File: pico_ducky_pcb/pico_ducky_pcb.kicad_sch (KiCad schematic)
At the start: 32 parts, among them J1 USB_A, J2 Conn_01x03_Female, SW1 R-667799, SW2 R-667799, U1 AP2127K-3.3, U2 W25Q32JVZP, U3 RP2040, Y1 Crystal_GND24

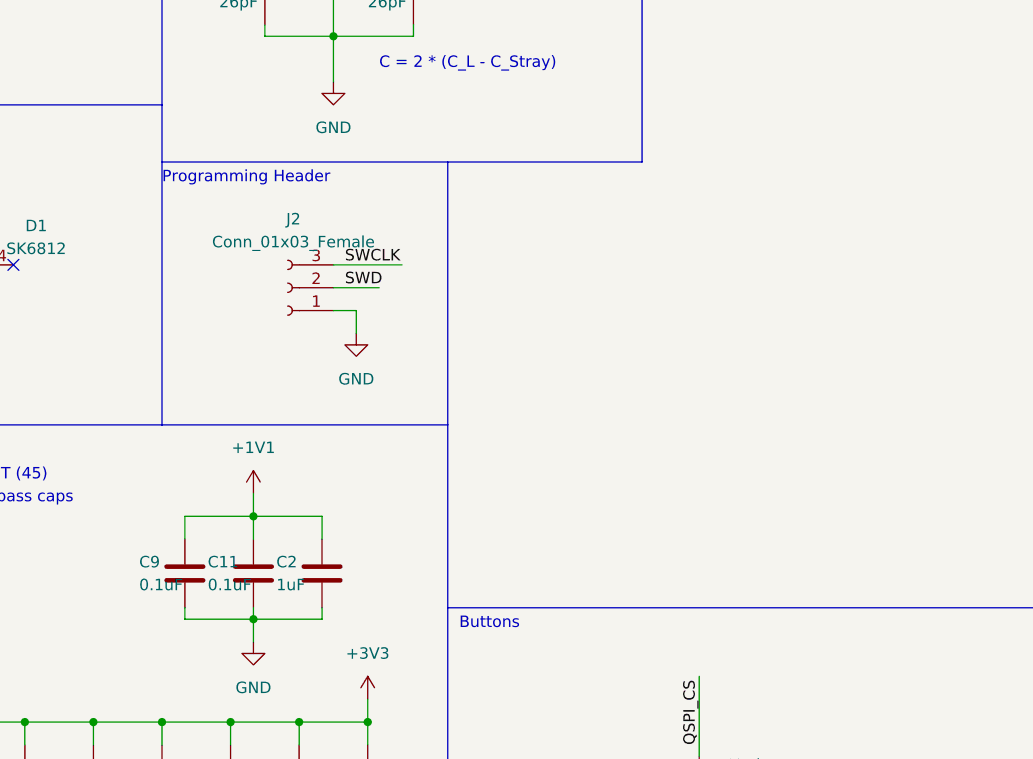
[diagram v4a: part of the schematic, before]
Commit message: fix silk screen adnd use 10 pin JTAG programmer
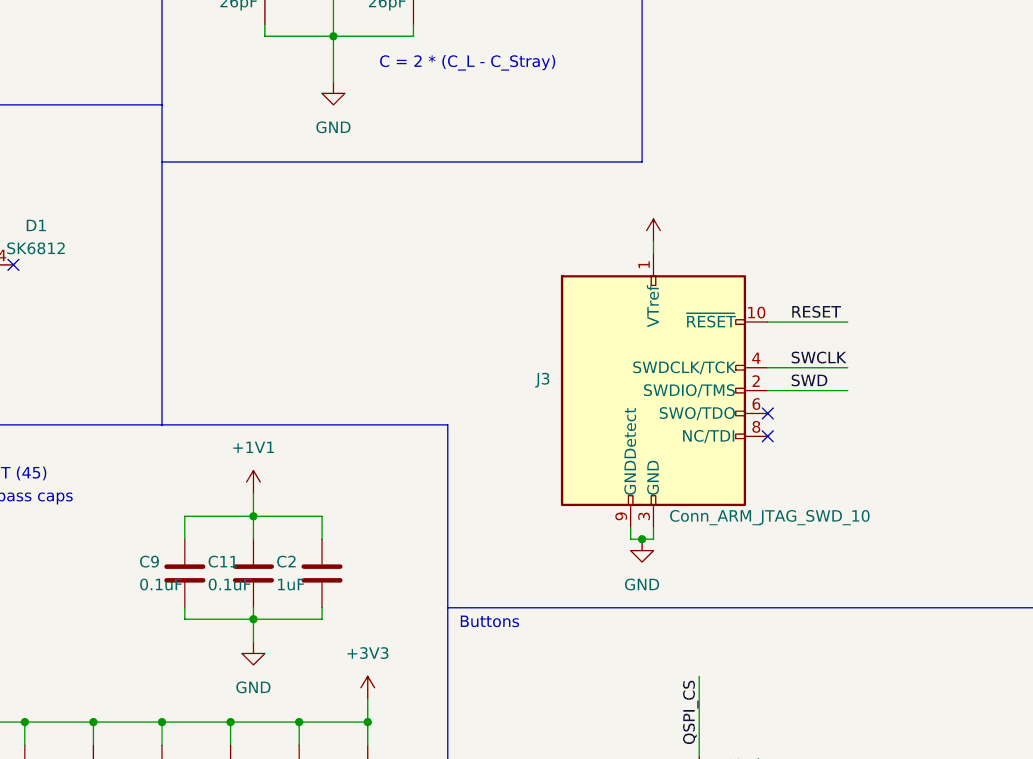
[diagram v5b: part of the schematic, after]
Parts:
- removed J2: Conn_01x03_Female, Connector_PinHeader_1.27mm:PinHeader_1x03_P1.27mm_Vertical, symbol Connector:Conn_01x03_Female
- added J3: Conn_ARM_JTAG_SWD_10, Connector_PinHeader_1.27mm:PinHeader_2x05_P1.27mm_Vertical, symbol Connector:Conn_ARM_JTAG_SWD_10
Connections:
- net +3V3: now also J3.1 (VTref)
- net GND: now also J3.3 (GND), J3.5 (GND), J3.9 (GNDDetect)
- net RESET: now also J3.10 (~{RESET})
- net SWCLK: now also J3.4 (SWDCLK/TCK)
- net SWD: now also J3.2 (SWDIO/TMS)
- no-connect marks 29 -> 31
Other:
- note removed: "Programming Header"
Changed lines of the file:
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@@
   (junction (at 222.25 43.18) (diameter 0) (color 0 0 0 0)
+  )
+  (junction (at 115.57 139.7) (diameter 0) (color 0 0 0 0)
   )
   (junction (at 138.43 187.96) (diameter 0) (color 0 0 0 0)
@@
   (no_connect (at 250.19 87.63))
   (no_connect (at 250.19 90.17))
+  (no_connect (at 129.54 125.73))
+  (no_connect (at 129.54 128.27))
   (no_connect (at 250.19 64.77))
   (no_connect (at 250.19 67.31))
@@
     (stroke (width 0) (type default) (color 0 0 0 0))
   )
-  (polyline (pts (xy 93.98 127) (xy 93.98 97.79))
-    (stroke (width 0) (type default) (color 0 0 0 0))
-  )
   (wire (pts (xy 177.8 118.11) (xy 186.69 118.11))
     (stroke (width 0) (type default) (color 0 0 0 0))
@@
     (stroke (width 0) (type default) (color 0 0 0 0))
   )
-  (wire (pts (xy 81.28 109.22) (xy 88.9 109.22))
-    (stroke (width 0) (type default) (color 0 0 0 0))
-  )
   (wire (pts (xy 85.09 171.45) (xy 77.47 171.45))
     (stroke (width 0) (type default) (color 0 0 0 0))
   )
-  (wire (pts (xy 83.82 114.3) (xy 83.82 116.84))
-    (stroke (width 0) (type default) (color 0 0 0 0))
-  )
   (wire (pts (xy 90.17 73.66) (xy 90.17 74.93))
     (stroke (width 0) (type default) (color 0 0 0 0))
@@
     (stroke (width 0) (type default) (color 0 0 0 0))
   )
+  (wire (pts (xy 115.57 139.7) (xy 116.84 139.7))
+    (stroke (width 0) (type default) (color 0 0 0 0))
+  )
   (wire (pts (xy 80.01 137.16) (xy 80.01 139.7))
     (stroke (width 0) (type default) (color 0 0 0 0))
@@
     (stroke (width 0) (type default) (color 0 0 0 0))
   )
+  (wire (pts (xy 129.54 115.57) (xy 138.43 115.57))
+    (stroke (width 0) (type default) (color 0 0 0 0))
+  )
   (polyline (pts (xy 62.23 12.7) (xy 62.23 46.99))
     (stroke (width 0) (type default) (color 0 0 0 0))
@@
     (stroke (width 0) (type default) (color 0 0 0 0))
   )
+  (wire (pts (xy 129.54 120.65) (xy 138.43 120.65))
+    (stroke (width 0) (type default) (color 0 0 0 0))
+  )
   (wire (pts (xy 99.06 182.88) (xy 99.06 187.96))
     (stroke (width 0) (type default) (color 0 0 0 0))
@@
     (stroke (width 0) (type default) (color 0 0 0 0))
   )
-  (wire (pts (xy 81.28 111.76) (xy 86.36 111.76))
+  (wire (pts (xy 114.3 138.43) (xy 114.3 139.7))
     (stroke (width 0) (type default) (color 0 0 0 0))
   )
@@
     (stroke (width 0) (type default) (color 0 0 0 0))
   )
-  (wire (pts (xy 81.28 114.3) (xy 83.82 114.3))
-    (stroke (width 0) (type default) (color 0 0 0 0))
-  )
   (wire (pts (xy 257.81 57.15) (xy 265.43 57.15))
     (stroke (width 0) (type default) (color 0 0 0 0))
@@
     (stroke (width 0) (type default) (color 0 0 0 0))
   )
+  (wire (pts (xy 129.54 123.19) (xy 138.43 123.19))
+    (stroke (width 0) (type default) (color 0 0 0 0))
+  )
   (wire (pts (xy 222.25 40.64) (xy 222.25 43.18))
     (stroke (width 0) (type default) (color 0 0 0 0))
@@
     (stroke (width 0) (type default) (color 0 0 0 0))
   )
+  (wire (pts (xy 116.84 139.7) (xy 116.84 138.43))
+    (stroke (width 0) (type default) (color 0 0 0 0))
+  )
   (wire (pts (xy 77.47 170.18) (xy 77.47 171.45))
     (stroke (width 0) (type default) (color 0 0 0 0))
@@
     (stroke (width 0) (type default) (color 0 0 0 0))
   )
+  (wire (pts (xy 114.3 139.7) (xy 115.57 139.7))
+    (stroke (width 0) (type default) (color 0 0 0 0))
+  )
   (wire (pts (xy 27.94 26.67) (xy 27.94 29.21))
     (stroke (width 0) (type default) (color 0 0 0 0))
@@
     (stroke (width 0) (type default) (color 0 0 0 0))
   )
+  (wire (pts (xy 116.84 106.68) (xy 116.84 107.95))
+    (stroke (width 0) (type default) (color 0 0 0 0))
+  )
   (wire (pts (xy 40.64 67.31) (xy 40.64 64.77))
     (stroke (width 0) (type default) (color 0 0 0 0))
@@
   )
   (text "C = 2 * (C_L - C_Stray)" (at 86.36 87.63 0)
-    (effects (font (size 1.27 1.27)) (justify left bottom))
-  )
-  (text "Programming Header" (at 62.23 100.33 0)
     (effects (font (size 1.27 1.27)) (justify left bottom))
   )
@@
     (effects (font (size 1.27 1.27)) (justify left bottom))
   )
-  (label "SWD" (at 82.55 111.76 0)
-    (effects (font (size 1.27 1.27)) (justify left bottom))
-  )
   (label "X_OUT" (at 100.33 73.66 0)
     (effects (font (size 1.27 1.27)) (justify left bottom))
   )
+  (label "RESET" (at 132.08 115.57 0)
+    (effects (font (size 1.27 1.27)) (justify left bottom))
+  )
   (label "QSPI_CS" (at 78.74 33.02 0)
     (effects (font (size 1.27 1.27)) (justify left bottom))
@@
     (effects (font (size 1.27 1.27)) (justify left bottom))
   )
-  (label "SWCLK" (at 82.55 109.22 0)
+  (label "SWD" (at 132.08 123.19 0)
     (effects (font (size 1.27 1.27)) (justify left bottom))
   )
@@
   )
   (label "USB_-" (at 38.1 74.93 0)
+    (effects (font (size 1.27 1.27)) (justify left bottom))
+  )
+  (label "SWCLK" (at 132.08 120.65 0)
     (effects (font (size 1.27 1.27)) (justify left bottom))
   )
@@
     (pin "1")
     (pin "2")
-  )
-  (symbol (lib_id "power:GND") (at 83.82 116.84 0) (unit 1)
-    (in_bom yes) (on_board yes) (fields_autoplaced)
-    (property "Reference" "#PWR0124" (id 0) (at 83.82 123.19 0)
-      (effects (font (size 1.27 1.27)) hide)
-    )
-    (property "Value" "GND" (id 1) (at 83.82 121.92 0))
-    (property "Footprint" "" (id 2) (at 83.82 116.84 0)
-      (effects (font (size 1.27 1.27)) hide)
-    )
-    (property "Datasheet" "" (id 3) (at 83.82 116.84 0)
-      (effects (font (size 1.27 1.27)) hide)
-    )
-    (pin "1")
   )
   (symbol (lib_id "Device:Crystal_GND24") (at 81.28 73.66 180) (unit 1)
@@
     (pin "G")
   )
+  (symbol (lib_id "power:GND") (at 115.57 139.7 0) (unit 1)
+    (in_bom yes) (on_board yes) (fields_autoplaced)
+    (property "Reference" "#PWR0124" (id 0) (at 115.57 146.05 0)
+      (effects (font (size 1.27 1.27)) hide)
+    )
+    (property "Value" "GND" (id 1) (at 115.57 144.78 0))
+    (property "Footprint" "" (id 2) (at 115.57 139.7 0)
+      (effects (font (size 1.27 1.27)) hide)
+    )
+    (property "Datasheet" "" (id 3) (at 115.57 139.7 0)
+      (effects (font (size 1.27 1.27)) hide)
+    )
+    (pin "1")
+  )
   (symbol (lib_id "Diode:NSR0320") (at 121.92 175.26 90) (unit 1)
     (in_bom yes) (on_board yes) (fields_autoplaced)
@@
     (pin "1")
   )
+  (symbol (lib_id "Connector:Conn_ARM_JTAG_SWD_10") (at 116.84 123.19 0) (unit 1)
+    (in_bom yes) (on_board yes)
+    (property "Reference" "J3" (id 0) (at 105.41 121.9199 0)
+      (effects (font (size 1.27 1.27)) (justify right))
+    )
+    (property "Value" "Conn_ARM_JTAG_SWD_10" (id 1) (at 140.97 137.16 0)
+      (effects (font (size 1.27 1.27)) (justify right))
+    )
+    (property "Footprint" "Connector_PinHeader_1.27mm:PinHeader_2x05_P1.27mm_Vertical" (id 2) (at 116.84 123.19 0)
+      (effects (font (size 1.27 1.27)) hide)
+    )
+    (property "Datasheet" "http://infocenter.arm.com/help/topic/com.arm.doc.ddi0314h/DDI0314H_coresight_components_trm.pdf" (id 3) (at 107.95 154.94 90)
+      (effects (font (size 1.27 1.27)) hide)
+    )
+    (pin "1")
+    (pin "10")
+    (pin "2")
+    (pin "3")
+    (pin "4")
+    (pin "5")
+    (pin "6")
+    (pin "7")
+    (pin "8")
+    (pin "9")
+  )
   (symbol (lib_id "Device:R_Small") (at 255.27 57.15 90) (unit 1)
     (in_bom yes) (on_board yes)
@@
     (pin "2")
   )
-  (symbol (lib_id "Connector:Conn_01x03_Female") (at 76.2 111.76 180) (unit 1)
-    (in_bom yes) (on_board yes) (fields_autoplaced)
-    (property "Reference" "J2" (id 0) (at 76.835 104.14 0))
-    (property "Value" "Conn_01x03_Female" (id 1) (at 76.835 106.68 0))
-    (property "Footprint" "Connector_PinHeader_1.27mm:PinHeader_1x03_P1.27mm_Vertical" (id 2) (at 76.2 111.76 0)
-      (effects (font (size 1.27 1.27)) hide)
-    )
-    (property "Datasheet" "~" (id 3) (at 76.2 111.76 0)
-      (effects (font (size 1.27 1.27)) hide)
-    )
-    (pin "1")
-    (pin "2")
-    (pin "3")
-  )
   (symbol (lib_id "Connector:USB_A") (at 30.48 72.39 0) (unit 1)
     (in_bom yes) (on_board yes) (fields_autoplaced)
@@
     (pin "5")
   )
+  (symbol (lib_id "power:+3V3") (at 116.84 106.68 0) (unit 1)
+    (in_bom yes) (on_board yes) (fields_autoplaced)
+    (property "Reference" "#PWR0127" (id 0) (at 116.84 110.49 0)
+      (effects (font (size 1.27 1.27)) hide)
+    )
+    (property "Value" "" (id 1) (at 116.84 101.6 0))
+    (property "Footprint" "" (id 2) (at 116.84 106.68 0)
+      (effects (font (size 1.27 1.27)) hide)
+    )
+    (property "Datasheet" "" (id 3) (at 116.84 106.68 0)
+      (effects (font (size 1.27 1.27)) hide)
+    )
+    (pin "1")
+  )
   (symbol (lib_id "power:+5V") (at 40.64 64.77 0) (unit 1)
     (in_bom yes) (on_board yes) (fields_autoplaced)
@@
       (reference "#PWR0123") (unit 1) (value "+3V3") (footprint "")
     )
-    (path "/3bf593e9-c2c3-42c2-96d2-9d25b633c24f"
+    (path "/9623c7f5-b982-4a97-9884-8edf78d23dd5"
       (reference "#PWR0124") (unit 1) (value "GND") (footprint "")
     )
@@
       (reference "#PWR0126") (unit 1) (value "+3V3") (footprint "")
     )
+    (path "/f55b2315-ffcf-45cb-b8d5-dd0439b81933"
+      (reference "#PWR0127") (unit 1) (value "+3V3") (footprint "")
+    )
     (path "/8a1748bd-f0bb-4572-a1dd-52c0f6327c17"
       (reference "C1") (unit 1) (value "1uF") (footprint "Capacitor_SMD:C_0402_1005Metric")
@@
       (reference "J1") (unit 1) (value "USB_A") (footprint "Connector_USB:USB_A_CNCTech_1001-011-01101_Horizontal")
     )
-    (path "/ec04fa47-027a-4b7b-b069-efb5e36e176f"
-      (reference "J2") (unit 1) (value "Conn_01x03_Female") (footprint "Connector_PinHeader_1.27mm:PinHeader_1x03_P1.27mm_Vertical")
+    (path "/c9cb9c6c-6b12-4cd5-9021-7e17c6632c17"
+      (reference "J3") (unit 1) (value "Conn_ARM_JTAG_SWD_10") (footprint "Connector_PinHeader_1.27mm:PinHeader_2x05_P1.27mm_Vertical")
     )
     (path "/c679408f-ba66-4be7-8d3b-6f996095fe80"

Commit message: just leave the project behind in the v1 folder
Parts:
- removed C3: 0.1uF, Capacitor_SMD:C_0201_0603Metric, symbol Device:C
- C5, C8: footprint Capacitor_SMD:C_0201_0603Metric -> Capacitor_SMD:C_0402_1005Metric
- R2: value 10k -> DNP
- U2: footprint 8-UFDFN:W25Q80DVUXIE TR -> Package_SON:USON-8_3x4mm_P0.4mm
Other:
- moved on the sheet: C14
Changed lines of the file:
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@@
   (junction (at 227.33 43.18) (diameter 0) (color 0 0 0 0)
   )
-  (junction (at 39.37 160.02) (diameter 0) (color 0 0 0 0)
-  )
   (junction (at 27.94 83.82) (diameter 0) (color 0 0 0 0)
   )
@@
   )
   (junction (at 85.09 160.02) (diameter 0) (color 0 0 0 0)
-  )
-  (junction (at 39.37 171.45) (diameter 0) (color 0 0 0 0)
   )
   (junction (at 121.92 185.42) (diameter 0) (color 0 0 0 0)
@@
     (stroke (width 0) (type default) (color 0 0 0 0))
   )
-  (wire (pts (xy 31.75 160.02) (xy 31.75 162.56))
-    (stroke (width 0) (type default) (color 0 0 0 0))
-  )
   (wire (pts (xy 177.8 118.11) (xy 186.69 118.11))
     (stroke (width 0) (type default) (color 0 0 0 0))
@@
     (stroke (width 0) (type default) (color 0 0 0 0))
   )
-  (wire (pts (xy 39.37 171.45) (xy 31.75 171.45))
-    (stroke (width 0) (type default) (color 0 0 0 0))
-  )
   (wire (pts (xy 71.12 35.56) (xy 71.12 34.29))
     (stroke (width 0) (type default) (color 0 0 0 0))
@@
     (stroke (width 0) (type default) (color 0 0 0 0))
   )
-  (wire (pts (xy 31.75 160.02) (xy 39.37 160.02))
-    (stroke (width 0) (type default) (color 0 0 0 0))
-  )
   (wire (pts (xy 205.74 43.18) (xy 200.66 43.18))
     (stroke (width 0) (type default) (color 0 0 0 0))
@@
   )
   (wire (pts (xy 224.79 43.18) (xy 227.33 43.18))
-    (stroke (width 0) (type default) (color 0 0 0 0))
-  )
-  (wire (pts (xy 31.75 170.18) (xy 31.75 171.45))
     (stroke (width 0) (type default) (color 0 0 0 0))
   )
@@
       (effects (font (size 1.27 1.27)) (justify right))
     )
-    (property "Footprint" "Capacitor_SMD:C_0201_0603Metric" (id 2) (at 70.1548 35.56 0)
+    (property "Footprint" "Capacitor_SMD:C_0402_1005Metric" (id 2) (at 70.1548 35.56 0)
       (effects (font (size 1.27 1.27)) hide)
     )
@@
     (pin "9")
   )
-  (symbol (lib_id "Device:C") (at 31.75 166.37 180) (unit 1)
-    (in_bom yes) (on_board yes)
-    (property "Reference" "C14" (id 0) (at 26.67 165.1 0)
-      (effects (font (size 1.27 1.27)) (justify right))
-    )
-    (property "Value" "1uF" (id 1) (at 26.67 167.64 0)
-      (effects (font (size 1.27 1.27)) (justify right))
-    )
-    (property "Footprint" "Capacitor_SMD:C_0402_1005Metric" (id 2) (at 30.7848 162.56 0)
-      (effects (font (size 1.27 1.27)) hide)
-    )
-    (property "Datasheet" "~" (id 3) (at 31.75 166.37 0)
+  (symbol (lib_id "Device:C") (at 39.37 166.37 180) (unit 1)
+    (in_bom yes) (on_board yes)
+    (property "Reference" "C14" (id 0) (at 34.29 165.1 0)
+      (effects (font (size 1.27 1.27)) (justify right))
+    )
+    (property "Value" "1uF" (id 1) (at 34.29 167.64 0)
+      (effects (font (size 1.27 1.27)) (justify right))
+    )
+    (property "Footprint" "Capacitor_SMD:C_0402_1005Metric" (id 2) (at 38.4048 162.56 0)
+      (effects (font (size 1.27 1.27)) hide)
+    )
+    (property "Datasheet" "~" (id 3) (at 39.37 166.37 0)
       (effects (font (size 1.27 1.27)) hide)
     )
@@
       (effects (font (size 1.27 1.27)) (justify left))
     )
-    (property "Footprint" "8-UFDFN:W25Q80DVUXIE TR" (id 2) (at 105.41 35.56 0)
+    (property "Footprint" "Package_SON:USON-8_3x4mm_P0.4mm" (id 2) (at 105.41 35.56 0)
       (effects (font (size 1.27 1.27)) hide)
     )
@@
     (in_bom yes) (on_board yes)
     (property "Reference" "R2" (id 0) (at 85.09 29.21 90))
-    (property "Value" "10k" (id 1) (at 87.63 27.94 90))
+    (property "Value" "DNP" (id 1) (at 87.63 27.94 90))
     (property "Footprint" "Resistor_SMD:R_0402_1005Metric" (id 2) (at 90.17 27.94 0)
       (effects (font (size 1.27 1.27)) hide)
@@
       (effects (font (size 1.27 1.27)) (justify right))
     )
-    (property "Footprint" "Capacitor_SMD:C_0201_0603Metric" (id 2) (at 61.2648 162.56 0)
+    (property "Footprint" "Capacitor_SMD:C_0402_1005Metric" (id 2) (at 61.2648 162.56 0)
       (effects (font (size 1.27 1.27)) hide)
     )
@@
       (effects (font (size 1.27 1.27)) hide)
     )
-    (property "Value" "" (id 1) (at 116.84 101.6 0))
+    (property "Value" "+3V3" (id 1) (at 116.84 101.6 0))
     (property "Footprint" "" (id 2) (at 116.84 106.68 0)
       (effects (font (size 1.27 1.27)) hide)
@@
     )
     (pin "1")
-  )
-  (symbol (lib_id "Device:C") (at 39.37 166.37 180) (unit 1)
-    (in_bom yes) (on_board yes)
-    (property "Reference" "C3" (id 0) (at 34.29 165.1 0)
-      (effects (font (size 1.27 1.27)) (justify right))
-    )
-    (property "Value" "0.1uF" (id 1) (at 34.29 167.64 0)
-      (effects (font (size 1.27 1.27)) (justify right))
-    )
-    (property "Footprint" "Capacitor_SMD:C_0201_0603Metric" (id 2) (at 38.4048 162.56 0)
-      (effects (font (size 1.27 1.27)) hide)
-    )
-    (property "Datasheet" "~" (id 3) (at 39.37 166.37 0)
-      (effects (font (size 1.27 1.27)) hide)
-    )
-    (pin "1")
-    (pin "2")
   )
   (sheet_instances
@@
       (reference "C2") (unit 1) (value "1uF") (footprint "Capacitor_SMD:C_0402_1005Metric")
     )
-    (path "/ffe743db-176e-4144-babe-66f1ed3050a1"
-      (reference "C3") (unit 1) (value "0.1uF") (footprint "Capacitor_SMD:C_0201_0603Metric")
-    )
     (path "/2a511aed-1dc0-49f6-a6e8-072f83d9c64d"
       (reference "C4") (unit 1) (value "0.1uF") (footprint "Capacitor_SMD:C_0201_0603Metric")
     )
     (path "/479e2ec2-9712-4822-9c99-fe7c38372dd6"
-      (reference "C5") (unit 1) (value "0.1uF") (footprint "Capacitor_SMD:C_0201_0603Metric")
+      (reference "C5") (unit 1) (value "0.1uF") (footprint "Capacitor_SMD:C_0402_1005Metric")
     )
     (path "/31e08a8a-8df5-4991-a2b2-737d58b6fa96"
@@
     )
     (path "/e3f151d0-e0c5-4e9e-8098-f5d5e50665a4"
-      (reference "C8") (unit 1) (value "0.1uF") (footprint "Capacitor_SMD:C_0201_0603Metric")
+      (reference "C8") (unit 1) (value "0.1uF") (footprint "Capacitor_SMD:C_0402_1005Metric")
     )
     (path "/8326f61a-1320-41ed-a615-1f04d649db79"
@@
     )
     (path "/c679408f-ba66-4be7-8d3b-6f996095fe80"
-      (reference "R2") (unit 1) (value "10k") (footprint "Resistor_SMD:R_0402_1005Metric")
+      (reference "R2") (unit 1) (value "DNP") (footprint "Resistor_SMD:R_0402_1005Metric")
     )
     (path "/1fa6e3d4-ed6a-45aa-b12d-58ffcaf26a3e"
@@
     )
     (path "/754eb9e9-dcdc-4c20-b31d-b8365e6de61c"
-      (reference "U2") (unit 1) (value "W25Q32JVZP") (footprint "8-UFDFN:W25Q80DVUXIE TR")
+      (reference "U2") (unit 1) (value "W25Q32JVZP") (footprint "Package_SON:USON-8_3x4mm_P0.4mm")
     )
     (path "/576070f0-5571-497b-b8a0-5fc48462f78c"
